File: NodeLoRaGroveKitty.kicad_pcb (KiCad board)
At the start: 2 copper layers, 45 x 50 mm, 42 parts, among them P1 PICKIT PROGRAMMER, P2 Battery, P3 A0, P4 D9, P5 USB-Serial, P6 I2C, SW1 SW_BOOT, SW2 SW_RESET, U1 AP2112, U2 MCP73831T-2ATI/OT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

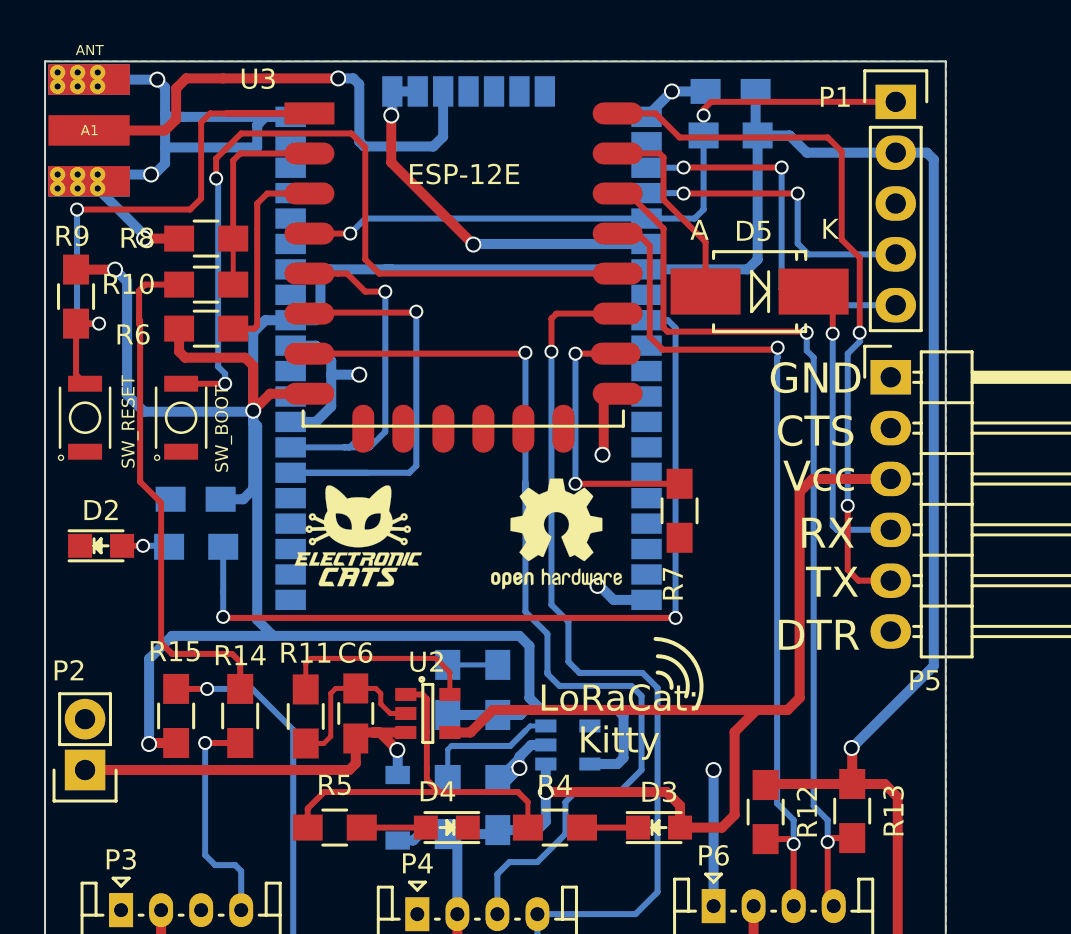
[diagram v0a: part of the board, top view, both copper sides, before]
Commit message: Update logos
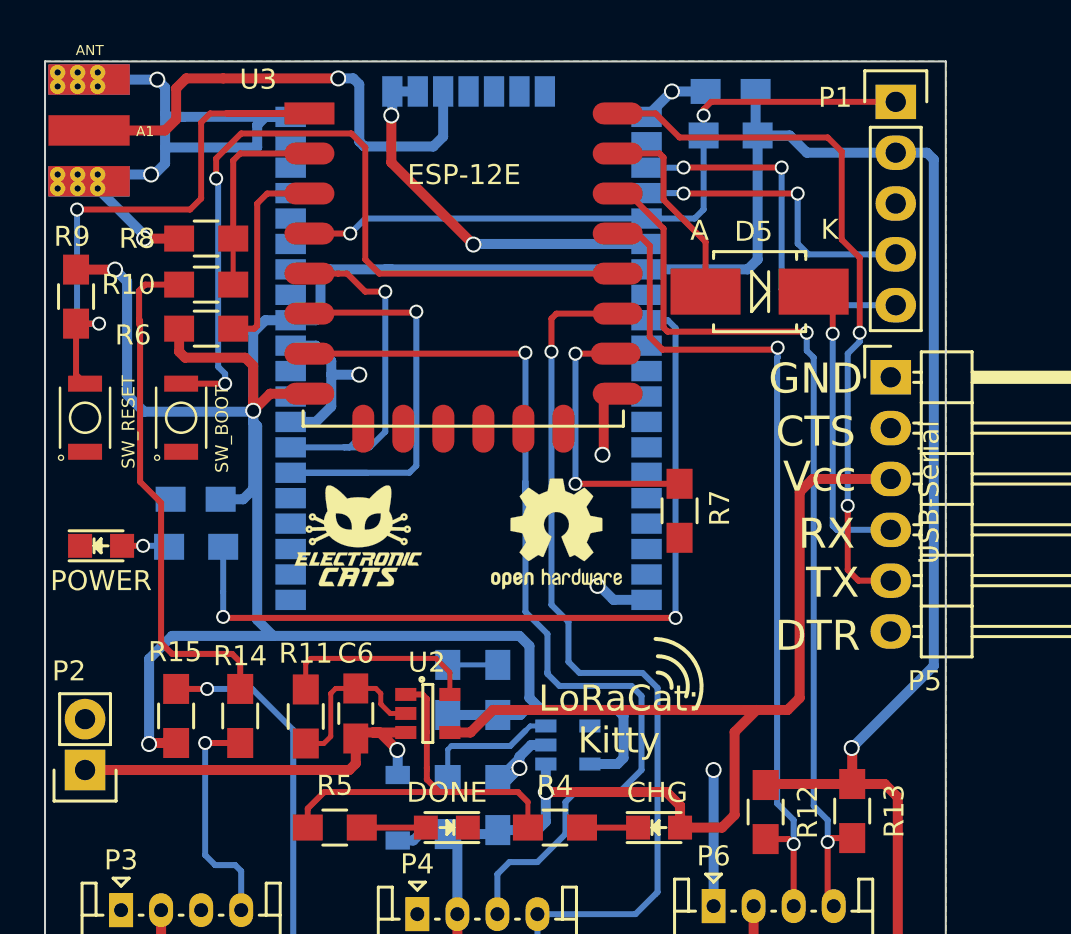
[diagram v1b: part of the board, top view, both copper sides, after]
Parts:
- D2: value Led -> POWER
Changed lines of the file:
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@@
   (general
     (links 109)
-    (no_connects 2)
+    (no_connects 1)
     (area 101.949999 96.949999 147.050001 147.050001)
     (thickness 1.6)
@@
   )
   (layers
-    (0 F.Cu signal)
-    (31 B.Cu signal)
+    (0 F.Cu signal hide)
+    (31 B.Cu signal hide)
     (32 B.Adhes user)
     (33 F.Adhes user)
@@
   (module TIH:GSG-SMA-EDGE (layer F.Cu)
     (at 106.232 100.45 180)
-    (fp_text reference A1 (at 1.99898 0 180) (layer F.SilkS)
+    (fp_text reference A1 (at -0.768 -0.05 180) (layer F.SilkS)
       (effects (font (size 0.50038 0.50038) (thickness 0.12446)))
     )
@@
     (tags "LED 0805 SMD")
     (attr smd)
-    (fp_text reference D2 (at 0 -1.75) (layer F.SilkS)
-      (effects (font (size 1 1) (thickness 0.15)))
-    )
-    (fp_text value Led (at 0 1.75) (layer F.Fab)
+    (fp_text reference D2 (at 0 -1.75) (layer F.Fab)
+      (effects (font (size 1 1) (thickness 0.15)))
+    )
+    (fp_text value POWER (at 0 1.75) (layer F.SilkS)
       (effects (font (size 1 1) (thickness 0.15)))
     )
@@
     (tags "LED 0805 SMD")
     (attr smd)
-    (fp_text reference D3 (at 0 -1.75) (layer F.SilkS)
-      (effects (font (size 1 1) (thickness 0.15)))
-    )
-    (fp_text value CHG (at 0 1.75) (layer F.Fab)
+    (fp_text reference D3 (at 0 -1.75) (layer F.Fab)
+      (effects (font (size 1 1) (thickness 0.15)))
+    )
+    (fp_text value CHG (at -0.085 -1.745) (layer F.SilkS)
       (effects (font (size 1 1) (thickness 0.15)))
     )
@@
     (tags "LED 0805 SMD")
     (attr smd)
-    (fp_text reference D4 (at 0.475 1.775 180) (layer F.SilkS)
-      (effects (font (size 1 1) (thickness 0.15)))
-    )
-    (fp_text value DONE (at 0 1.75 180) (layer F.Fab)
+    (fp_text reference D4 (at 0.475 1.775 180) (layer F.Fab)
+      (effects (font (size 1 1) (thickness 0.15)))
+    )
+    (fp_text value DONE (at 0 1.75 180) (layer F.SilkS)
       (effects (font (size 1 1) (thickness 0.15)))
     )
@@
       (effects (font (size 1 1) (thickness 0.15)))
     )
-    (fp_text value USB-Serial (at 2.692 6.032 90) (layer F.Fab)
+    (fp_text value USB-Serial (at 1.92 5.74 90) (layer F.SilkS)
       (effects (font (size 1 1) (thickness 0.15)))
     )
@@
     (tags "resistor 0805")
     (attr smd)
-    (fp_text reference R7 (at 3.65 0.3 270) (layer F.SilkS)
+    (fp_text reference R7 (at -0.14 -2.01 270) (layer F.SilkS)
       (effects (font (size 1 1) (thickness 0.15)))
     )
@@
   (gr_arc (start 132.425 128.225) (end 132.5 125.85) (angle 115.4908253) (layer F.SilkS) (width 0.2))
   (gr_text GND (at 108 129.8) (layer B.SilkS)
-    (effects (font (size 1.5 1.5) (thickness 0.3)))
+    (effects (font (size 1.5 1.5) (thickness 0.3)) (justify mirror))
   )
   (gr_text "+Batt\n" (at 108.95 132.45) (layer B.SilkS)
-    (effects (font (size 1.5 1.5) (thickness 0.3)))
+    (effects (font (size 1.5 1.5) (thickness 0.3)) (justify mirror))
   )
   (gr_text DTR (at 140.6 125.7) (layer F.SilkS)

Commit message: Fix bug footprint
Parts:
- removed RN2903: RN2903, Library:RN2483
- added MODULE1: RN2903, TIH:RN2483, B.Cu at (132.0, 125.1)
- D2: value POWER -> Led
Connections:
- U3 pad 5: /S_TX -> /STX
- U3 pad 6: /S_RX -> /SRX
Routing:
- net +3V3: track 230.8 -> 147.5 mm, vias 4 -> 3
- net GND: track 90.9 -> 141.7 mm, vias 11 -> 8
- net (no net): track 0.00 -> 48.4 mm, vias 0 -> 5
- net /S_RX/GPIO12: track 18.0 -> 0.00 mm, vias 1 -> 0
- net /S_TX/GPIO14: track 13.7 -> 0.00 mm, vias 1 -> 0
- net /S_RX: track 4.61 -> 0.00 mm
- net VCC: track 64.9 -> 61.4 mm
- net /S_TX: track 2.46 -> 0.00 mm
- net /STX: track 0.00 -> 2.46 mm
- net Net-(MODULE1-Pad36): track 42.2 -> 44.2 mm

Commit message: Fix re-bug
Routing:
- net +3V3: track 147.5 -> 230.8 mm, vias 3 -> 4
- net (no net): track 48.4 -> 0.00 mm, vias 5 -> 0
- net GND: track 141.7 -> 100.3 mm, vias 8 -> 13
- net /SRX: track 0.07 -> 22.8 mm, vias 0 -> 1
- net /STX: track 2.46 -> 15.7 mm, vias 0 -> 1
- net Net-(MODULE1-Pad36): track 44.2 -> 42.2 mm
- net /RX: track 10.6 -> 11.3 mm

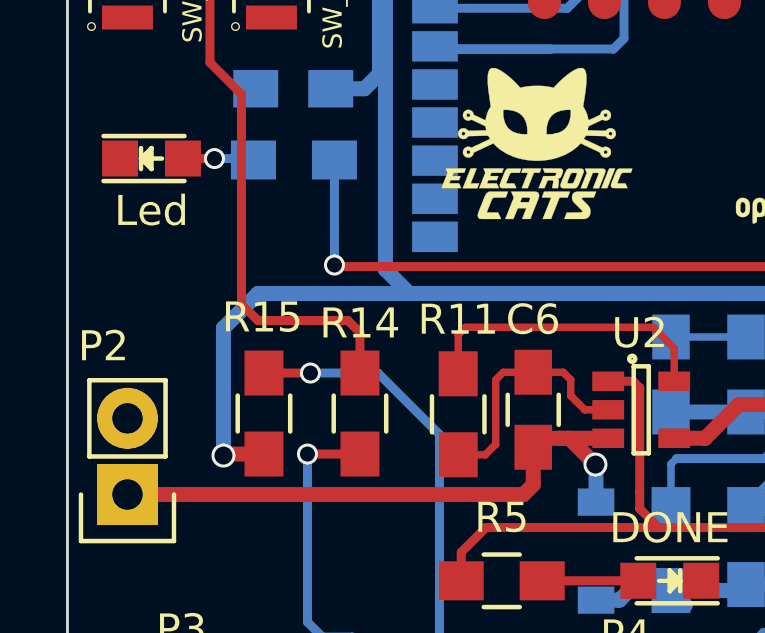
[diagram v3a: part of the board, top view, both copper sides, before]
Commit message: Update logos
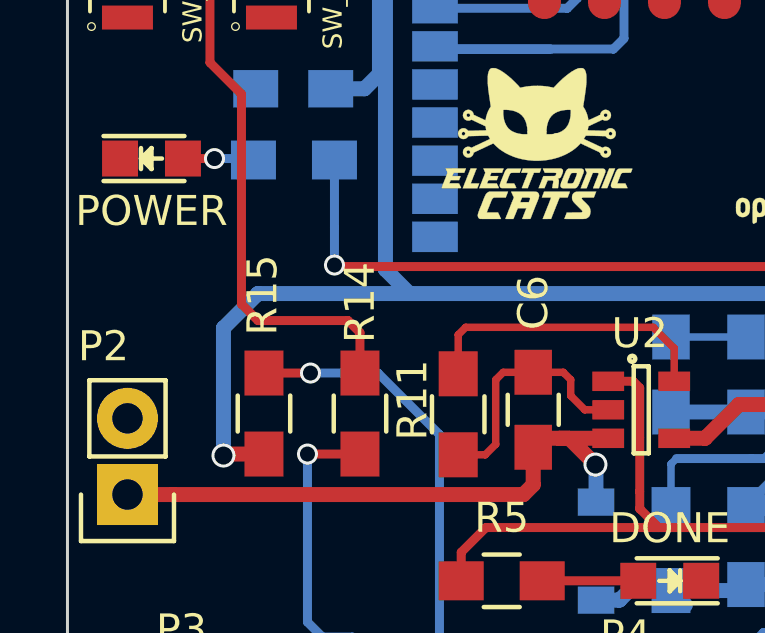
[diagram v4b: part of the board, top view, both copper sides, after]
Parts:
- D2: value Led -> POWER
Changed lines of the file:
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@@
   (general
     (links 111)
-    (no_connects 1)
-    (area 81.150001 72.3 155.125001 148.175)
+    (no_connects 0)
+    (area 101.949999 96.949999 147.050001 147.050001)
     (thickness 1.6)
     (drawings 21)
@@
   )
   (layers
-    (0 F.Cu signal)
-    (31 B.Cu signal)
+    (0 F.Cu signal hide)
+    (31 B.Cu signal hide)
     (32 B.Adhes user)
     (33 F.Adhes user)
@@
     (tags "capacitor 0805")
     (attr smd)
-    (fp_text reference C6 (at 3 0 180) (layer F.SilkS)
+    (fp_text reference C6 (at 3.575 0 270) (layer F.SilkS)
       (effects (font (size 1 1) (thickness 0.15)))
     )
@@
       (effects (font (size 1 1) (thickness 0.15)))
     )
-    (fp_text value Led (at 0 1.75) (layer F.SilkS)
+    (fp_text value POWER (at 0 1.75) (layer F.SilkS)
       (effects (font (size 1 1) (thickness 0.15)))
     )
@@
     (tags "resistor 0805")
     (attr smd)
-    (fp_text reference R11 (at -3.15 0 360) (layer F.SilkS)
+    (fp_text reference R11 (at -0.475 1.525 450) (layer F.SilkS)
       (effects (font (size 1 1) (thickness 0.15)))
     )
@@
     (tags "resistor 0805")
     (attr smd)
-    (fp_text reference R14 (at 3 0 180) (layer F.SilkS)
+    (fp_text reference R14 (at 3.7 0 270) (layer F.SilkS)
       (effects (font (size 1 1) (thickness 0.15)))
     )
@@
     (tags "resistor 0805")
     (attr smd)
-    (fp_text reference R15 (at 3.2 -0.05 180) (layer F.SilkS)
-      (effects (font (size 1 1) (thickness 0.15)))
-    )
+    (fp_text reference R15 (at 3.95 -0.05 270) (layer F.SilkS)
+      (effects (font (size 1 1) (thickness 0.15)))
+    )

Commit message: Update BOM
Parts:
- D2: value POWER -> Led
- P5: footprint Pin_Headers:Pin_Header_Angled_1x06 -> Socket_Strips:Socket_Strip_Straight_1x06
- turned P5 to 270 degrees
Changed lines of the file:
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@@
     (links 111)
     (no_connects 0)
-    (area 101.949999 96.949999 147.050001 147.050001)
+    (area 81.150001 72.3 152.485714 148.175)
     (thickness 1.6)
     (drawings 21)
@@
   )
   (layers
-    (0 F.Cu signal hide)
-    (31 B.Cu signal hide)
+    (0 F.Cu signal)
+    (31 B.Cu signal)
     (32 B.Adhes user)
     (33 F.Adhes user)
@@
       (drillshape 0)
       (scaleselection 1)
-      (outputdirectory "../Tarjetas Produccion/Gerbers_161215/LoRaKitty/"))
+      (outputdirectory "../Tarjetas Produccion/Gerbers_170109/LoRaKitty/"))
   )
   (net 0 "")
@@
       (effects (font (size 1 1) (thickness 0.15)))
     )
-    (fp_text value POWER (at 0 1.75) (layer F.SilkS)
+    (fp_text value Led (at 0 1.75) (layer F.SilkS)
       (effects (font (size 1 1) (thickness 0.15)))
     )
@@
     (pad 4 thru_hole oval (at 6 0) (size 1.2 1.7) (drill 0.7) (layers *.Cu *.Mask F.SilkS)
       (net 56 /GPIO2))
-  )
-  (module Pin_Headers:Pin_Header_Angled_1x06 (layer F.Cu)
-    (at 144.25 112.78)
-    (descr "Through hole pin header")
-    (tags "pin header")
-    (fp_text reference P5 (at 1.7 15.17) (layer F.SilkS)
-      (effects (font (size 1 1) (thickness 0.15)))
-    )
-    (fp_text value USB-Serial (at 1.92 5.74 90) (layer F.SilkS)
-      (effects (font (size 1 1) (thickness 0.15)))
-    )
-    (fp_line (start -1.5 -1.75) (end -1.5 14.45) (layer F.CrtYd) (width 0.05))
-    (fp_line (start 10.65 -1.75) (end 10.65 14.45) (layer F.CrtYd) (width 0.05))
-    (fp_line (start -1.5 -1.75) (end 10.65 -1.75) (layer F.CrtYd) (width 0.05))
-    (fp_line (start -1.5 14.45) (end 10.65 14.45) (layer F.CrtYd) (width 0.05))
-    (fp_line (start -1.3 -1.55) (end -1.3 0) (layer F.SilkS) (width 0.15))
-    (fp_line (start 0 -1.55) (end -1.3 -1.55) (layer F.SilkS) (width 0.15))
-    (fp_line (start 4.191 -0.127) (end 10.033 -0.127) (layer F.SilkS) (width 0.15))
-    (fp_line (start 10.033 -0.127) (end 10.033 0.127) (layer F.SilkS) (width 0.15))
-    (fp_line (start 10.033 0.127) (end 4.191 0.127) (layer F.SilkS) (width 0.15))
-    (fp_line (start 4.191 0.127) (end 4.191 0) (layer F.SilkS) (width 0.15))
-    (fp_line (start 4.191 0) (end 10.033 0) (layer F.SilkS) (width 0.15))
-    (fp_line (start 1.524 -0.254) (end 1.143 -0.254) (layer F.SilkS) (width 0.15))
-    (fp_line (start 1.524 0.254) (end 1.143 0.254) (layer F.SilkS) (width 0.15))
-    (fp_line (start 1.524 2.286) (end 1.143 2.286) (layer F.SilkS) (width 0.15))
-    (fp_line (start 1.524 2.794) (end 1.143 2.794) (layer F.SilkS) (width 0.15))
-    (fp_line (start 1.524 4.826) (end 1.143 4.826) (layer F.SilkS) (width 0.15))
-    (fp_line (start 1.524 5.334) (end 1.143 5.334) (layer F.SilkS) (width 0.15))
-    (fp_line (start 1.524 12.954) (end 1.143 12.954) (layer F.SilkS) (width 0.15))
-    (fp_line (start 1.524 12.446) (end 1.143 12.446) (layer F.SilkS) (width 0.15))
-    (fp_line (start 1.524 10.414) (end 1.143 10.414) (layer F.SilkS) (width 0.15))
-    (fp_line (start 1.524 9.906) (end 1.143 9.906) (layer F.SilkS) (width 0.15))
-    (fp_line (start 1.524 7.874) (end 1.143 7.874) (layer F.SilkS) (width 0.15))
-    (fp_line (start 1.524 7.366) (end 1.143 7.366) (layer F.SilkS) (width 0.15))
-    (fp_line (start 1.524 -1.27) (end 4.064 -1.27) (layer F.SilkS) (width 0.15))
-    (fp_line (start 1.524 1.27) (end 4.064 1.27) (layer F.SilkS) (width 0.15))
-    (fp_line (start 1.524 1.27) (end 1.524 3.81) (layer F.SilkS) (width 0.15))
-    (fp_line (start 1.524 3.81) (end 4.064 3.81) (layer F.SilkS) (width 0.15))
-    (fp_line (start 4.064 2.286) (end 10.16 2.286) (layer F.SilkS) (width 0.15))
-    (fp_line (start 10.16 2.286) (end 10.16 2.794) (layer F.SilkS) (width 0.15))
-    (fp_line (start 10.16 2.794) (end 4.064 2.794) (layer F.SilkS) (width 0.15))
-    (fp_line (start 4.064 3.81) (end 4.064 1.27) (layer F.SilkS) (width 0.15))
-    (fp_line (start 4.064 1.27) (end 4.064 -1.27) (layer F.SilkS) (width 0.15))
-    (fp_line (start 10.16 0.254) (end 4.064 0.254) (layer F.SilkS) (width 0.15))
-    (fp_line (start 10.16 -0.254) (end 10.16 0.254) (layer F.SilkS) (width 0.15))
-    (fp_line (start 4.064 -0.254) (end 10.16 -0.254) (layer F.SilkS) (width 0.15))
-    (fp_line (start 1.524 1.27) (end 4.064 1.27) (layer F.SilkS) (width 0.15))
-    (fp_line (start 1.524 -1.27) (end 1.524 1.27) (layer F.SilkS) (width 0.15))
-    (fp_line (start 1.524 8.89) (end 4.064 8.89) (layer F.SilkS) (width 0.15))
-    (fp_line (start 1.524 8.89) (end 1.524 11.43) (layer F.SilkS) (width 0.15))
-    (fp_line (start 1.524 11.43) (end 4.064 11.43) (layer F.SilkS) (width 0.15))
-    (fp_line (start 4.064 9.906) (end 10.16 9.906) (layer F.SilkS) (width 0.15))
-    (fp_line (start 10.16 9.906) (end 10.16 10.414) (layer F.SilkS) (width 0.15))
-    (fp_line (start 10.16 10.414) (end 4.064 10.414) (layer F.SilkS) (width 0.15))
-    (fp_line (start 4.064 11.43) (end 4.064 8.89) (layer F.SilkS) (width 0.15))
-    (fp_line (start 4.064 13.97) (end 4.064 11.43) (layer F.SilkS) (width 0.15))
-    (fp_line (start 10.16 12.954) (end 4.064 12.954) (layer F.SilkS) (width 0.15))
-    (fp_line (start 10.16 12.446) (end 10.16 12.954) (layer F.SilkS) (width 0.15))
-    (fp_line (start 4.064 12.446) (end 10.16 12.446) (layer F.SilkS) (width 0.15))
-    (fp_line (start 1.524 13.97) (end 4.064 13.97) (layer F.SilkS) (width 0.15))
-    (fp_line (start 1.524 11.43) (end 1.524 13.97) (layer F.SilkS) (width 0.15))
-    (fp_line (start 1.524 11.43) (end 4.064 11.43) (layer F.SilkS) (width 0.15))
-    (fp_line (start 1.524 6.35) (end 4.064 6.35) (layer F.SilkS) (width 0.15))
-    (fp_line (start 1.524 6.35) (end 1.524 8.89) (layer F.SilkS) (width 0.15))
-    (fp_line (start 1.524 8.89) (end 4.064 8.89) (layer F.SilkS) (width 0.15))
-    (fp_line (start 4.064 7.366) (end 10.16 7.366) (layer F.SilkS) (width 0.15))
-    (fp_line (start 10.16 7.366) (end 10.16 7.874) (layer F.SilkS) (width 0.15))
-    (fp_line (start 10.16 7.874) (end 4.064 7.874) (layer F.SilkS) (width 0.15))
-    (fp_line (start 4.064 8.89) (end 4.064 6.35) (layer F.SilkS) (width 0.15))
-    (fp_line (start 4.064 6.35) (end 4.064 3.81) (layer F.SilkS) (width 0.15))
-    (fp_line (start 10.16 5.334) (end 4.064 5.334) (layer F.SilkS) (width 0.15))
-    (fp_line (start 10.16 4.826) (end 10.16 5.334) (layer F.SilkS) (width 0.15))
-    (fp_line (start 4.064 4.826) (end 10.16 4.826) (layer F.SilkS) (width 0.15))
-    (fp_line (start 1.524 6.35) (end 4.064 6.35) (layer F.SilkS) (width 0.15))
-    (fp_line (start 1.524 3.81) (end 1.524 6.35) (layer F.SilkS) (width 0.15))
-    (fp_line (start 1.524 3.81) (end 4.064 3.81) (layer F.SilkS) (width 0.15))
-    (pad 1 thru_hole rect (at 0 0) (size 2.032 1.7272) (drill 1.016) (layers *.Cu *.Mask F.SilkS)
-      (net 2 GND))
-    (pad 2 thru_hole oval (at 0 2.54) (size 2.032 1.7272) (drill 1.016) (layers *.Cu *.Mask F.SilkS)
-      (net 37 "Net-(P5-Pad2)"))
-    (pad 3 thru_hole oval (at 0 5.08) (size 2.032 1.7272) (drill 1.016) (layers *.Cu *.Mask F.SilkS)
-      (net 3 VCC))
-    (pad 4 thru_hole oval (at 0 7.62) (size 2.032 1.7272) (drill 1.016) (layers *.Cu *.Mask F.SilkS)
-      (net 9 /RX_5V))
-    (pad 5 thru_hole oval (at 0 10.16) (size 2.032 1.7272) (drill 1.016) (layers *.Cu *.Mask F.SilkS)
-      (net 38 /TX))
-    (pad 6 thru_hole oval (at 0 12.7) (size 2.032 1.7272) (drill 1.016) (layers *.Cu *.Mask F.SilkS)
-      (net 39 "Net-(P5-Pad6)"))
-    (model Pin_Headers.3dshapes/Pin_Header_Angled_1x06.wrl
-      (at (xyz 0 -0.25 0))
-      (scale (xyz 1 1 1))
-      (rotate (xyz 0 0 90))
-    )
   )
   (module Connectors_JST:JST_PH_S4B-PH-K_04x2.00mm_Angled (layer F.Cu)
@@
       (net 2 GND))
   )
+  (module Socket_Strips:Socket_Strip_Straight_1x06 (layer F.Cu)
+    (at 144.272 112.776 270)
+    (descr "Through hole socket strip")
+    (tags "socket strip")
+    (fp_text reference P5 (at 15.494 -0.254 270) (layer F.SilkS)
+      (effects (font (size 1 1) (thickness 0.15)))
+    )
+    (fp_text value USB-Serial (at 0 -3.1 270) (layer F.Fab)
+      (effects (font (size 1 1) (thickness 0.15)))
+    )
+    (fp_line (start -1.75 -1.75) (end -1.75 1.75) (layer F.CrtYd) (width 0.05))
+    (fp_line (start 14.45 -1.75) (end 14.45 1.75) (layer F.CrtYd) (width 0.05))
+    (fp_line (start -1.75 -1.75) (end 14.45 -1.75) (layer F.CrtYd) (width 0.05))
+    (fp_line (start -1.75 1.75) (end 14.45 1.75) (layer F.CrtYd) (width 0.05))
+    (fp_line (start 1.27 1.27) (end 13.97 1.27) (layer F.SilkS) (width 0.15))
+    (fp_line (start 13.97 1.27) (end 13.97 -1.27) (layer F.SilkS) (width 0.15))
+    (fp_line (start 13.97 -1.27) (end 1.27 -1.27) (layer F.SilkS) (width 0.15))
+    (fp_line (start -1.55 1.55) (end 0 1.55) (layer F.SilkS) (width 0.15))
+    (fp_line (start 1.27 1.27) (end 1.27 -1.27) (layer F.SilkS) (width 0.15))
+    (fp_line (start 0 -1.55) (end -1.55 -1.55) (layer F.SilkS) (width 0.15))
+    (fp_line (start -1.55 -1.55) (end -1.55 1.55) (layer F.SilkS) (width 0.15))
+    (pad 1 thru_hole rect (at 0 0 270) (size 1.7272 2.032) (drill 1.016) (layers *.Cu *.Mask)
+      (net 2 GND))
+    (pad 2 thru_hole oval (at 2.54 0 270) (size 1.7272 2.032) (drill 1.016) (layers *.Cu *.Mask)
+      (net 37 "Net-(P5-Pad2)"))
+    (pad 3 thru_hole oval (at 5.08 0 270) (size 1.7272 2.032) (drill 1.016) (layers *.Cu *.Mask)
+      (net 3 VCC))
+    (pad 4 thru_hole oval (at 7.62 0 270) (size 1.7272 2.032) (drill 1.016) (layers *.Cu *.Mask)
+      (net 9 /RX_5V))
+    (pad 5 thru_hole oval (at 10.16 0 270) (size 1.7272 2.032) (drill 1.016) (layers *.Cu *.Mask)
+      (net 38 /TX))
+    (pad 6 thru_hole oval (at 12.7 0 270) (size 1.7272 2.032) (drill 1.016) (layers *.Cu *.Mask)
+      (net 39 "Net-(P5-Pad6)"))
+    (model Socket_Strips.3dshapes/Socket_Strip_Straight_1x06.wrl
+      (at (xyz 0.25 0 0))
+      (scale (xyz 1 1 1))
+      (rotate (xyz 0 0 180))
+    )
+  )
   (gr_arc (start 132.603474 128.230347) (end 132.603474 127.530347) (angle 95.71059314) (layer F.SilkS) (width 0.2))

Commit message: Fix Rename pin D15 to D2
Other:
- board text added: "GND VCC D13 D2"
- board text removed: "GND VCC D13 D15"
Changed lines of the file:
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@@
   )
   (layers
-    (0 F.Cu signal)
-    (31 B.Cu signal)
+    (0 F.Cu signal hide)
+    (31 B.Cu signal hide)
     (32 B.Adhes user)
     (33 F.Adhes user)
@@
     (effects (font (size 1.5 1.5) (thickness 0.3)) (justify mirror))
   )
-  (gr_text "GND\nVCC\nD13\nD15" (at 123.952 143.256 90) (layer B.SilkS)
+  (gr_text "GND\nVCC\nD13\nD2" (at 123.952 143.256 90) (layer B.SilkS)
     (effects (font (size 1.5 1.5) (thickness 0.3)) (justify mirror))
   )
